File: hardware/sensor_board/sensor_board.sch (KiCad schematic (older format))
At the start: 4 parts, among them J0 Conn_01x04, U0 HIHxx3x-021

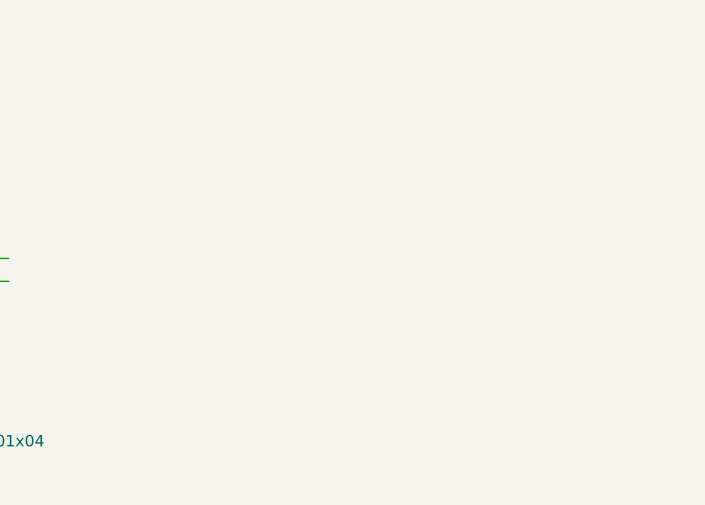
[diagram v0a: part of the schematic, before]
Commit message: Moving form multiplexer to two I2C busses
Changed from using one I2C bus with a multiplexer to using two I2C busses with the addition of level shifters
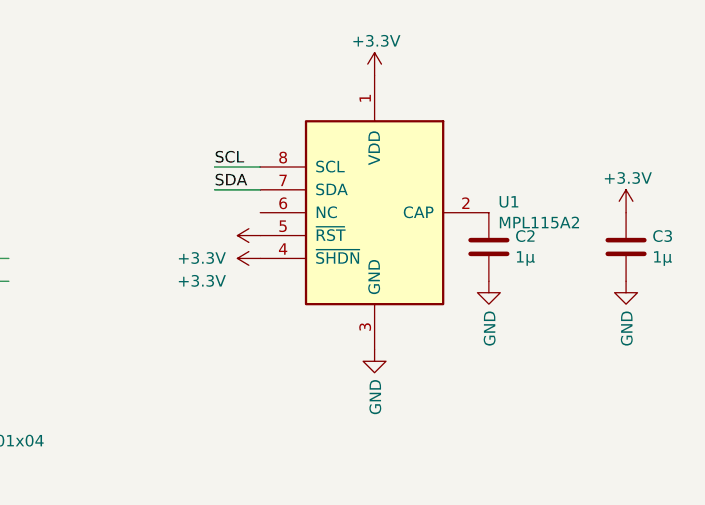
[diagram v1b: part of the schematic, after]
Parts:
- added C2, C3: 1µ, Capacitor_SMD:C_0805_2012Metric_Pad1.15x1.40mm_HandSolder, symbol Device:C
- added U1: MPL115A2, Package_LGA:LGA-8_3x5mm_P1.25mm, symbol Sensor_Pressure:MPL115A2
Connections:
- wire segments 6 -> 8
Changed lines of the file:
@@
 $EndComp
 $Comp
-L power:+3.3V #PWR?
+L power:+3.3V #PWR0103
 U 1 1 5C4785CE
 P 4300 4200
-F 0 "#PWR?" H 4300 4050 50  0001 C CNN
+F 0 "#PWR0103" H 4300 4050 50  0001 C CNN
 F 1 "+3.3V" H 4200 4350 50  0000 L CNN
 F 2 "" H 4300 4200 50  0001 C CNN
@@
 	1    0    0    -1
 $EndComp
+$Comp
+L Sensor_Pressure:MPL115A2 U1
+U 1 1 5C48755E
+P 6450 3400
+F 0 "U1" H 6991 3446 50  0000 L CNN
+F 1 "MPL115A2" H 6991 3355 50  0000 L CNN
+F 2 "Package_LGA:LGA-8_3x5mm_P1.25mm" H 6600 2700 50  0001 C CNN
+F 3 "http://www.nxp.com/assets/documents/data/en/data-sheets/MPL115A1.pdf" H 6450 3400 50  0001 C CNN
+	1    6450 3400
+	1    0    0    -1
+$EndComp
+$Comp
+L power:+3.3V #PWR0108
+U 1 1 5C487869
+P 6450 2800
+F 0 "#PWR0108" H 6450 2650 50  0001 C CNN
+F 1 "+3.3V" H 6350 2950 50  0000 L CNN
+F 2 "" H 6450 2800 50  0001 C CNN
+F 3 "" H 6450 2800 50  0001 C CNN
+	1    6450 2800
+	1    0    0    -1
+$EndComp
+$Comp
+L power:GND #PWR0109
+U 1 1 5C4878C6
+P 6450 4000
+F 0 "#PWR0109" H 6450 3750 50  0001 C CNN
+F 1 "GND" V 6455 3872 50  0000 R CNN
+F 2 "" H 6450 4000 50  0001 C CNN
+F 3 "" H 6450 4000 50  0001 C CNN
+	1    6450 4000
+	1    0    0    -1
+$EndComp
+Text Label 5750 3200 0    50   ~ 0
+SCL
+Wire Wire Line
+	5950 3200 5750 3200
+Text Label 5750 3300 0    50   ~ 0
+SDA
+Wire Wire Line
+	5950 3300 5750 3300
+$Comp
+L Device:C C2
+U 1 1 5C487C0F
+P 6950 3550
+F 0 "C2" H 7065 3596 50  0000 L CNN
+F 1 "1µ" H 7065 3505 50  0000 L CNN
+F 2 "Capacitor_SMD:C_0805_2012Metric_Pad1.15x1.40mm_HandSolder" H 6988 3400 50  0001 C CNN
+F 3 "~" H 6950 3550 50  0001 C CNN
+	1    6950 3550
+	1    0    0    -1
+$EndComp
+$Comp
+L Device:C C3
+U 1 1 5C487C4B
+P 7550 3550
+F 0 "C3" H 7665 3596 50  0000 L CNN
+F 1 "1µ" H 7665 3505 50  0000 L CNN
+F 2 "Capacitor_SMD:C_0805_2012Metric_Pad1.15x1.40mm_HandSolder" H 7588 3400 50  0001 C CNN
+F 3 "~" H 7550 3550 50  0001 C CNN
+	1    7550 3550
+	1    0    0    -1
+$EndComp
+$Comp
+L power:GND #PWR0110
+U 1 1 5C487E59
+P 6950 3700
+F 0 "#PWR0110" H 6950 3450 50  0001 C CNN
+F 1 "GND" V 6955 3572 50  0000 R CNN
+F 2 "" H 6950 3700 50  0001 C CNN
+F 3 "" H 6950 3700 50  0001 C CNN
+	1    6950 3700
+	1    0    0    -1
+$EndComp
+$Comp
+L power:GND #PWR0111
+U 1 1 5C487ED5
+P 7550 3700
+F 0 "#PWR0111" H 7550 3450 50  0001 C CNN
+F 1 "GND" V 7555 3572 50  0000 R CNN
+F 2 "" H 7550 3700 50  0001 C CNN
+F 3 "" H 7550 3700 50  0001 C CNN
+	1    7550 3700
+	1    0    0    -1
+$EndComp
+$Comp
+L power:+3.3V #PWR0112
+U 1 1 5C487F9C
+P 7550 3400
+F 0 "#PWR0112" H 7550 3250 50  0001 C CNN
+F 1 "+3.3V" H 7450 3550 50  0000 L CNN
+F 2 "" H 7550 3400 50  0001 C CNN
+F 3 "" H 7550 3400 50  0001 C CNN
+	1    7550 3400
+	1    0    0    -1
+$EndComp
+$Comp
+L power:+3.3V #PWR0113
+U 1 1 5C488294
+P 5950 3600
+F 0 "#PWR0113" H 5950 3450 50  0001 C CNN
+F 1 "+3.3V" V 5850 3750 50  0000 L CNN
+F 2 "" H 5950 3600 50  0001 C CNN
+F 3 "" H 5950 3600 50  0001 C CNN
+	1    5950 3600
+	0    -1   -1   0
+$EndComp
+$Comp
+L power:+3.3V #PWR0114
+U 1 1 5C4884EB
+P 5950 3500
+F 0 "#PWR0114" H 5950 3350 50  0001 C CNN
+F 1 "+3.3V" V 5850 3650 50  0000 L CNN
+F 2 "" H 5950 3500 50  0001 C CNN
+F 3 "" H 5950 3500 50  0001 C CNN
+	1    5950 3500
+	0    -1   -1   0
+$EndComp
 $EndSCHEMATC

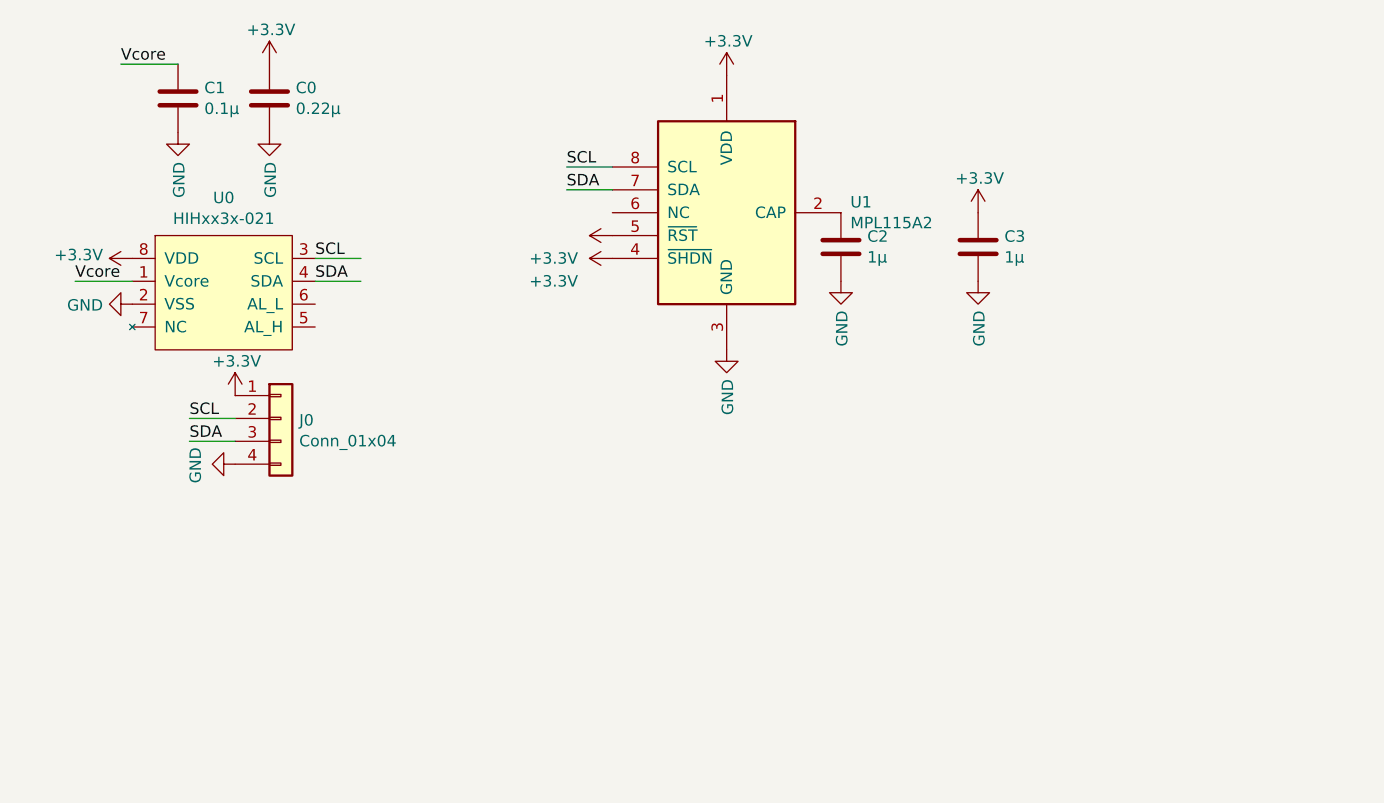
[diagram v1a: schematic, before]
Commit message: Sensor board v2 and improvements to pHAT
Added a I2C level shifter to the sensor board, which lead to a complete redesign
Some graphical improvements to the pHAT
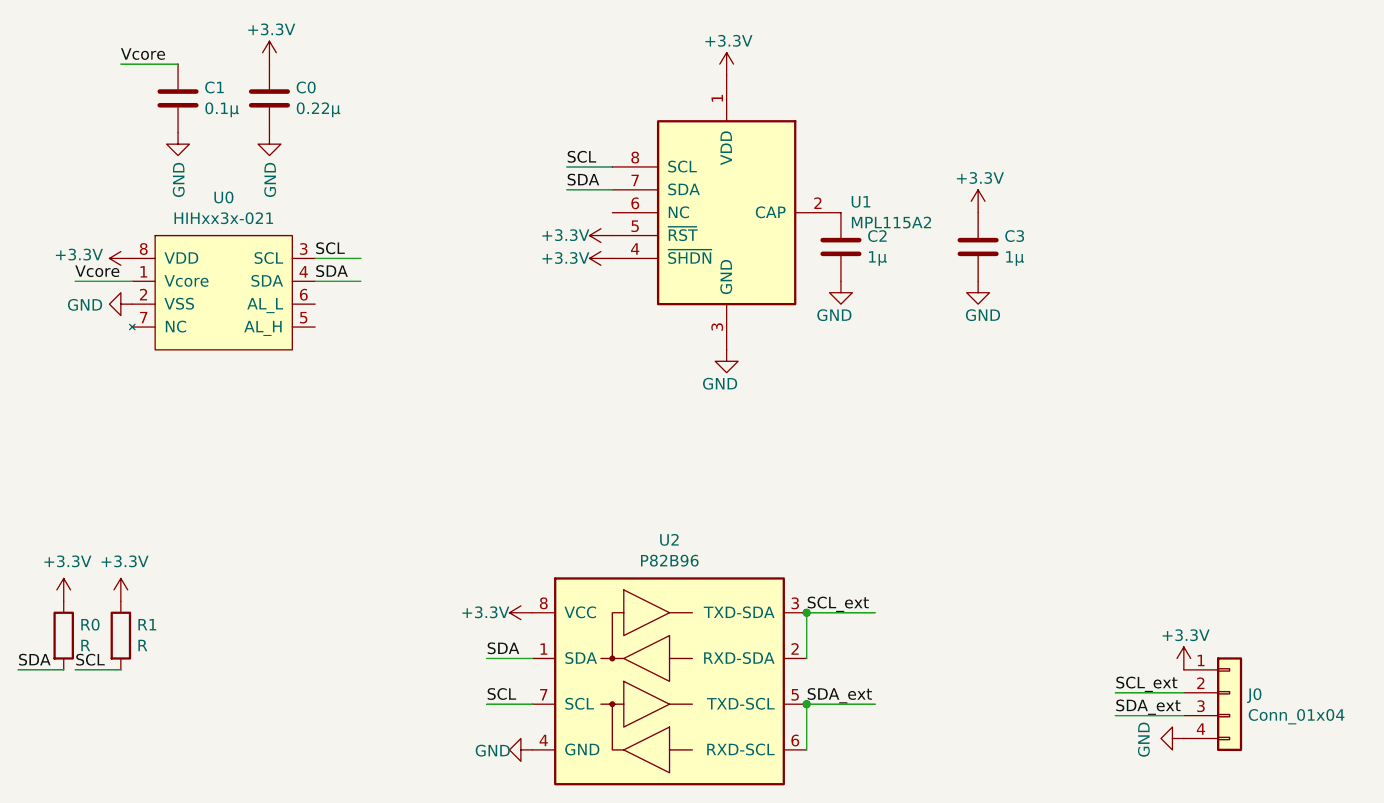
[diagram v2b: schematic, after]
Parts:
- added R0, R1: R, Resistor_SMD:R_0805_2012Metric_Pad1.15x1.40mm_HandSolder, symbol Device:R
- added U2: P82B96, Package_SO:SOIC-8_3.9x4.9mm_P1.27mm, symbol Interface_Expansion:P82B96
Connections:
- net labels added: SCL_ext, SDA_ext
- wire segments 8 -> 16
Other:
- moved on the sheet: J0
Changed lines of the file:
@@
 Title "Beehive Sensor board"
 Date "2019-01-22"
-Rev "v1.0"
+Rev "v2.0"
 Comp "University of Glasgow"
 Comment1 ""
@@
 L Connector_Generic:Conn_01x04 J0
 U 1 1 5C472B69
-P 4500 4300
-F 0 "J0" H 4580 4292 50  0000 L CNN
-F 1 "Conn_01x04" H 4580 4201 50  0000 L CNN
-F 2 "Connector_Molex:Molex_KK-254_AE-6410-04A_1x04_P2.54mm_Vertical" H 4500 4300 50  0001 C CNN
-F 3 "~" H 4500 4300 50  0001 C CNN
-	1    4500 4300
+P 8650 5500
+F 0 "J0" H 8730 5492 50  0000 L CNN
+F 1 "Conn_01x04" H 8730 5401 50  0000 L CNN
+F 2 "Connector_Molex:Molex_KK-254_AE-6410-04A_1x04_P2.54mm_Vertical" H 8650 5500 50  0001 C CNN
+F 3 "~" H 8650 5500 50  0001 C CNN
+	1    8650 5500
 	1    0    0    -1
 $EndComp
@@
 L power:GND #PWR0101
 U 1 1 5C472C56
-P 4300 4500
-F 0 "#PWR0101" H 4300 4250 50  0001 C CNN
-F 1 "GND" H 4305 4327 50  0000 C CNN
-F 2 "" H 4300 4500 50  0001 C CNN
-F 3 "" H 4300 4500 50  0001 C CNN
-	1    4300 4500
+P 8450 5700
+F 0 "#PWR0101" H 8450 5450 50  0001 C CNN
+F 1 "GND" H 8455 5527 50  0000 C CNN
+F 2 "" H 8450 5700 50  0001 C CNN
+F 3 "" H 8450 5700 50  0001 C CNN
+	1    8450 5700
 	0    1    1    0
 $EndComp
@@
 	0    -1   -1   0
 $EndComp
-Text Label 4100 4400 0    50   ~ 0
-SDA
-Text Label 4100 4300 0    50   ~ 0
-SCL
-Wire Wire Line
-	4300 4400 4100 4400
-Wire Wire Line
-	4300 4300 4100 4300
+Text Label 8150 5600 0    50   ~ 0
+SDA_ext
+Text Label 8150 5500 0    50   ~ 0
+SCL_ext
 Text Label 4650 3600 0    50   ~ 0
 SCL
@@
 L power:+3.3V #PWR0103
 U 1 1 5C4785CE
-P 4300 4200
-F 0 "#PWR0103" H 4300 4050 50  0001 C CNN
-F 1 "+3.3V" H 4200 4350 50  0000 L CNN
-F 2 "" H 4300 4200 50  0001 C CNN
-F 3 "" H 4300 4200 50  0001 C CNN
-	1    4300 4200
+P 8450 5400
+F 0 "#PWR0103" H 8450 5250 50  0001 C CNN
+F 1 "+3.3V" H 8350 5550 50  0000 L CNN
+F 2 "" H 8450 5400 50  0001 C CNN
+F 3 "" H 8450 5400 50  0001 C CNN
+	1    8450 5400
 	1    0    0    -1
 $EndComp
@@
 P 6450 4000
 F 0 "#PWR0109" H 6450 3750 50  0001 C CNN
-F 1 "GND" V 6455 3872 50  0000 R CNN
+F 1 "GND" H 6500 3850 50  0000 R CNN
 F 2 "" H 6450 4000 50  0001 C CNN
 F 3 "" H 6450 4000 50  0001 C CNN
@@
 P 6950 3700
 F 0 "#PWR0110" H 6950 3450 50  0001 C CNN
-F 1 "GND" V 6955 3572 50  0000 R CNN
+F 1 "GND" H 7000 3550 50  0000 R CNN
 F 2 "" H 6950 3700 50  0001 C CNN
 F 3 "" H 6950 3700 50  0001 C CNN
@@
 P 7550 3700
 F 0 "#PWR0111" H 7550 3450 50  0001 C CNN
-F 1 "GND" V 7555 3572 50  0000 R CNN
+F 1 "GND" H 7650 3550 50  0000 R CNN
 F 2 "" H 7550 3700 50  0001 C CNN
 F 3 "" H 7550 3700 50  0001 C CNN
@@
 P 5950 3600
 F 0 "#PWR0113" H 5950 3450 50  0001 C CNN
-F 1 "+3.3V" V 5850 3750 50  0000 L CNN
+F 1 "+3.3V" V 5950 3700 50  0000 L CNN
 F 2 "" H 5950 3600 50  0001 C CNN
 F 3 "" H 5950 3600 50  0001 C CNN
@@
 P 5950 3500
 F 0 "#PWR0114" H 5950 3350 50  0001 C CNN
-F 1 "+3.3V" V 5850 3650 50  0000 L CNN
+F 1 "+3.3V" V 5950 3600 50  0000 L CNN
 F 2 "" H 5950 3500 50  0001 C CNN
 F 3 "" H 5950 3500 50  0001 C CNN
@@
 	0    -1   -1   0
 $EndComp
+$Comp
+L Interface_Expansion:P82B96 U2
+U 1 1 5C4C662B
+P 6200 5450
+F 0 "U2" H 6200 6067 50  0000 C CNN
+F 1 "P82B96" H 6200 5976 50  0000 C CNN
+F 2 "Package_SO:SOIC-8_3.9x4.9mm_P1.27mm" H 6200 5450 50  0001 C CNN
+F 3 "http://www.nxp.com/documents/data_sheet/P82B96.pdf" H 6200 5450 50  0001 C CNN
+	1    6200 5450
+	1    0    0    -1
+$EndComp
+Wire Wire Line
+	8450 5500 8150 5500
+Wire Wire Line
+	8450 5600 8150 5600
+Text Label 6800 5550 0    50   ~ 0
+SDA_ext
+Text Label 6800 5150 0    50   ~ 0
+SCL_ext
+Wire Wire Line
+	7100 5150 6800 5150
+Wire Wire Line
+	7100 5550 6800 5550
+Wire Wire Line
+	6800 5150 6800 5350
+Connection ~ 6800 5150
+Wire Wire Line
+	6800 5550 6800 5750
+Connection ~ 6800 5550
+$Comp
+L power:GND #PWR0115
+U 1 1 5C4C70EE
+P 5600 5750
+F 0 "#PWR0115" H 5600 5500 50  0001 C CNN
+F 1 "GND" V 5605 5577 50  0000 C CNN
+F 2 "" H 5600 5750 50  0001 C CNN
+F 3 "" H 5600 5750 50  0001 C CNN
+	1    5600 5750
+	0    1    1    0
+$EndComp
+$Comp
+L power:+3.3V #PWR0116
+U 1 1 5C4C71BF
+P 5600 5150
+F 0 "#PWR0116" H 5600 5000 50  0001 C CNN
+F 1 "+3.3V" V 5600 5250 50  0000 L CNN
+F 2 "" H 5600 5150 50  0001 C CNN
+F 3 "" H 5600 5150 50  0001 C CNN
+	1    5600 5150
+	0    -1   -1   0
+$EndComp
+Text Label 5400 5550 0    50   ~ 0
+SCL
+Wire Wire Line
+	5600 5550 5400 5550
+Text Label 5400 5350 0    50   ~ 0
+SDA
+Wire Wire Line
+	5600 5350 5400 5350
+$Comp
+L Device:R R0
+U 1 1 5C4C91BE
+P 3550 5250
+F 0 "R0" H 3620 5296 50  0000 L CNN
+F 1 "R" H 3620 5205 50  0000 L CNN
+F 2 "Resistor_SMD:R_0805_2012Metric_Pad1.15x1.40mm_HandSolder" V 3480 5250 50  0001 C CNN
+F 3 "~" H 3550 5250 50  0001 C CNN
+	1    3550 5250
+	1    0    0    -1
+$EndComp
+$Comp
+L Device:R R1
+U 1 1 5C4C9224
+P 3800 5250
+F 0 "R1" H 3870 5296 50  0000 L CNN
+F 1 "R" H 3870 5205 50  0000 L CNN
+F 2 "Resistor_SMD:R_0805_2012Metric_Pad1.15x1.40mm_HandSolder" V 3730 5250 50  0001 C CNN
+F 3 "~" H 3800 5250 50  0001 C CNN
+	1    3800 5250
+	1    0    0    -1
+$EndComp
+$Comp
+L power:+3.3V #PWR0117
+U 1 1 5C4C957B
+P 3550 5100
+F 0 "#PWR0117" H 3550 4950 50  0001 C CNN
+F 1 "+3.3V" H 3565 5273 50  0000 C CNN
+F 2 "" H 3550 5100 50  0001 C CNN
+F 3 "" H 3550 5100 50  0001 C CNN
+	1    3550 5100
+	1    0    0    -1
+$EndComp
+$Comp
+L power:+3.3V #PWR0118
+U 1 1 5C4C95B1
+P 3800 5100
+F 0 "#PWR0118" H 3800 4950 50  0001 C CNN
+F 1 "+3.3V" H 3815 5273 50  0000 C CNN
+F 2 "" H 3800 5100 50  0001 C CNN
+F 3 "" H 3800 5100 50  0001 C CNN
+	1    3800 5100
+	1    0    0    -1
+$EndComp
+Text Label 3600 5400 0    50   ~ 0
+SCL
+Wire Wire Line
+	3800 5400 3600 5400
+Text Label 3350 5400 0    50   ~ 0
+SDA
+Wire Wire Line
+	3550 5400 3350 5400
 $EndSCHEMATC

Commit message: Added the alarm pin for humidity
Added support for the alarm pin of the HIH6131 in order to detect through interrupt a high level of humidity
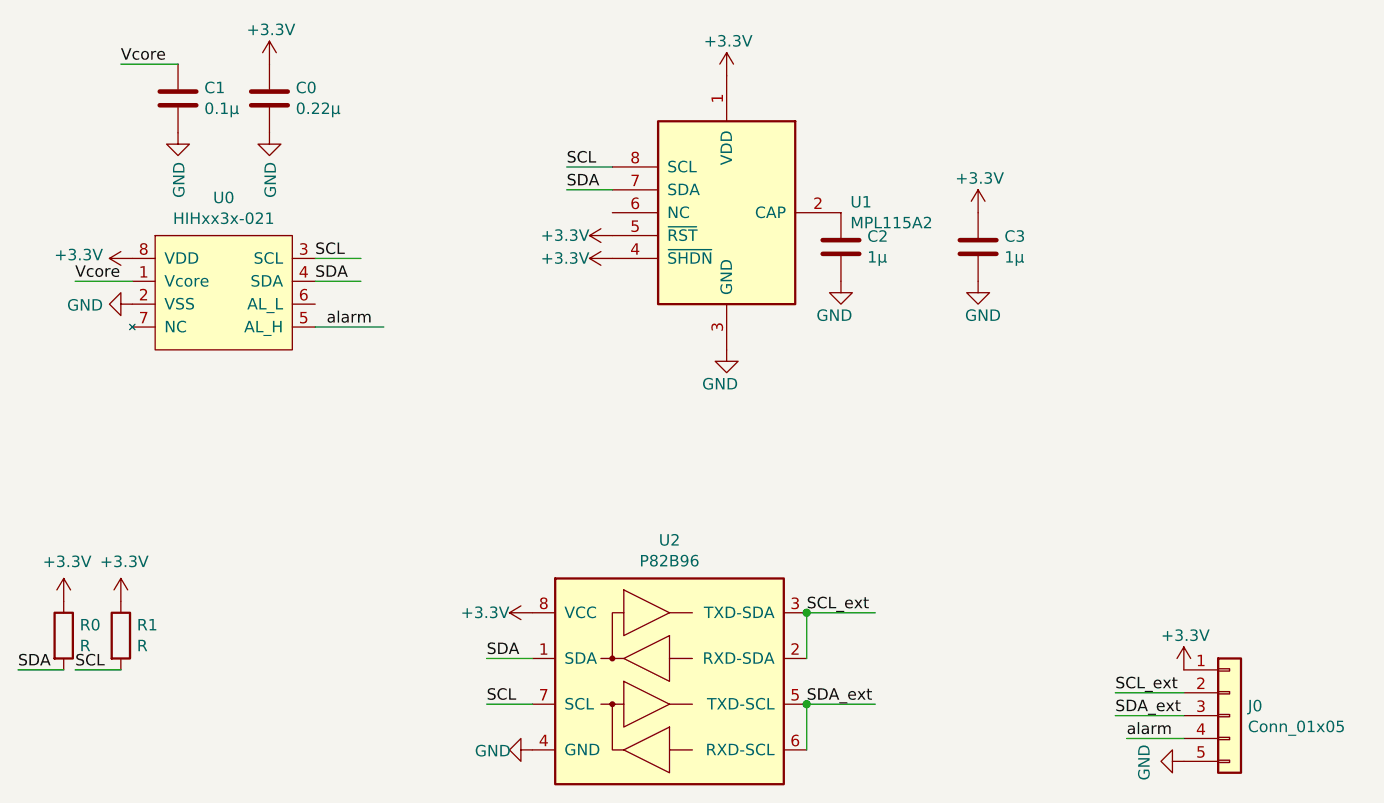
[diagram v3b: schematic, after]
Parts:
- removed J0: Conn_01x04, Connector_Molex:Molex_KK-254_AE-6410-04A_1x04_P2.54mm_Vertical, symbol Connector_Generic:Conn_01x04
- added J0: Conn_01x05, Connector_Molex:Molex_KK-254_AE-6410-05A_1x05_P2.54mm_Vertical, symbol Connector_Generic:Conn_01x05
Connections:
- net labels added: alarm
- wire segments 16 -> 18
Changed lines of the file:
@@
 Sheet 1 1
 Title "Beehive Sensor board"
-Date "2019-01-22"
-Rev "v2.0"
+Date "2019-01-29"
+Rev "v2.1"
 Comp "University of Glasgow"
 Comment1 ""
@@
 $EndComp
 $Comp
-L Connector_Generic:Conn_01x04 J0
-U 1 1 5C472B69
-P 8650 5500
-F 0 "J0" H 8730 5492 50  0000 L CNN
-F 1 "Conn_01x04" H 8730 5401 50  0000 L CNN
-F 2 "Connector_Molex:Molex_KK-254_AE-6410-04A_1x04_P2.54mm_Vertical" H 8650 5500 50  0001 C CNN
-F 3 "~" H 8650 5500 50  0001 C CNN
-	1    8650 5500
-	1    0    0    -1
-$EndComp
-$Comp
 L power:GND #PWR0101
 U 1 1 5C472C56
-P 8450 5700
-F 0 "#PWR0101" H 8450 5450 50  0001 C CNN
-F 1 "GND" H 8455 5527 50  0000 C CNN
-F 2 "" H 8450 5700 50  0001 C CNN
-F 3 "" H 8450 5700 50  0001 C CNN
-	1    8450 5700
+P 8450 5800
+F 0 "#PWR0101" H 8450 5550 50  0001 C CNN
+F 1 "GND" H 8455 5627 50  0000 C CNN
+F 2 "" H 8450 5800 50  0001 C CNN
+F 3 "" H 8450 5800 50  0001 C CNN
+	1    8450 5800
 	0    1    1    0
 $EndComp
@@
 Wire Wire Line
 	3550 5400 3350 5400
+$Comp
+L Connector_Generic:Conn_01x05 J0
+U 1 1 5C503B4A
+P 8650 5600
+F 0 "J0" H 8730 5642 50  0000 L CNN
+F 1 "Conn_01x05" H 8730 5551 50  0000 L CNN
+F 2 "Connector_Molex:Molex_KK-254_AE-6410-05A_1x05_P2.54mm_Vertical" H 8650 5600 50  0001 C CNN
+F 3 "~" H 8650 5600 50  0001 C CNN
+	1    8650 5600
+	1    0    0    -1
+$EndComp
+Wire Wire Line
+	4650 3900 4950 3900
+Text Label 4700 3900 0    50   ~ 0
+alarm
+Text Label 8200 5700 0    50   ~ 0
+alarm
+Wire Wire Line
+	8450 5700 8200 5700
 $EndSCHEMATC

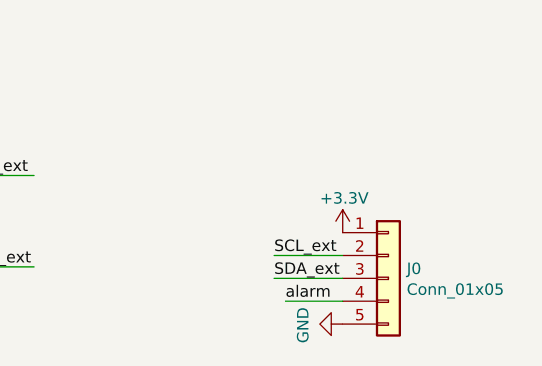
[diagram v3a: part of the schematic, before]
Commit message: Preparing layout for adding a fan
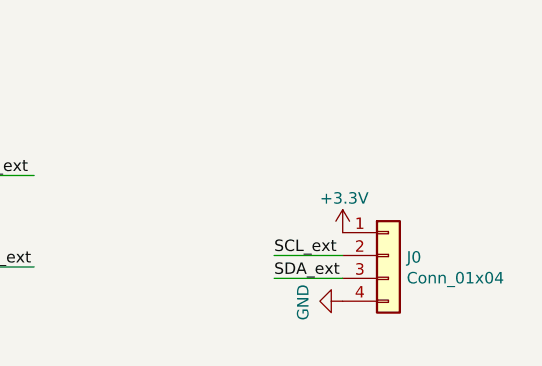
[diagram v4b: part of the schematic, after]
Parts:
- removed J0: Conn_01x05, Connector_Molex:Molex_KK-254_AE-6410-05A_1x05_P2.54mm_Vertical, symbol Connector_Generic:Conn_01x05
- added J0: Conn_01x04, Connector_Molex:Molex_KK-254_AE-6410-04A_1x04_P2.54mm_Vertical, symbol Connector_Generic:Conn_01x04
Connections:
- wire segments 18 -> 17
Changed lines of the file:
@@
 L power:GND #PWR0101
 U 1 1 5C472C56
-P 8450 5800
-F 0 "#PWR0101" H 8450 5550 50  0001 C CNN
-F 1 "GND" H 8455 5627 50  0000 C CNN
-F 2 "" H 8450 5800 50  0001 C CNN
-F 3 "" H 8450 5800 50  0001 C CNN
-	1    8450 5800
+P 8450 5700
+F 0 "#PWR0101" H 8450 5450 50  0001 C CNN
+F 1 "GND" H 8455 5527 50  0000 C CNN
+F 2 "" H 8450 5700 50  0001 C CNN
+F 3 "" H 8450 5700 50  0001 C CNN
+	1    8450 5700
 	0    1    1    0
 $EndComp
@@
 Wire Wire Line
 	3550 5400 3350 5400
-$Comp
-L Connector_Generic:Conn_01x05 J0
-U 1 1 5C503B4A
-P 8650 5600
-F 0 "J0" H 8730 5642 50  0000 L CNN
-F 1 "Conn_01x05" H 8730 5551 50  0000 L CNN
-F 2 "Connector_Molex:Molex_KK-254_AE-6410-05A_1x05_P2.54mm_Vertical" H 8650 5600 50  0001 C CNN
-F 3 "~" H 8650 5600 50  0001 C CNN
-	1    8650 5600
-	1    0    0    -1
-$EndComp
 Wire Wire Line
 	4650 3900 4950 3900
 Text Label 4700 3900 0    50   ~ 0
 alarm
-Text Label 8200 5700 0    50   ~ 0
-alarm
-Wire Wire Line
-	8450 5700 8200 5700
+$Comp
+L Connector_Generic:Conn_01x04 J0
+U 1 1 5C642F7D
+P 8650 5500
+F 0 "J0" H 8730 5492 50  0000 L CNN
+F 1 "Conn_01x04" H 8730 5401 50  0000 L CNN
+F 2 "Connector_Molex:Molex_KK-254_AE-6410-04A_1x04_P2.54mm_Vertical" H 8650 5500 50  0001 C CNN
+F 3 "~" H 8650 5500 50  0001 C CNN
+	1    8650 5500
+	1    0    0    -1
+$EndComp
 $EndSCHEMATC
